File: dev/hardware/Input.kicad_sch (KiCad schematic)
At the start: 23 parts, among them J601 Conn_02x08_Top_Bottom, SW1 TILT SW, U601 74HC165, U602 74HC165

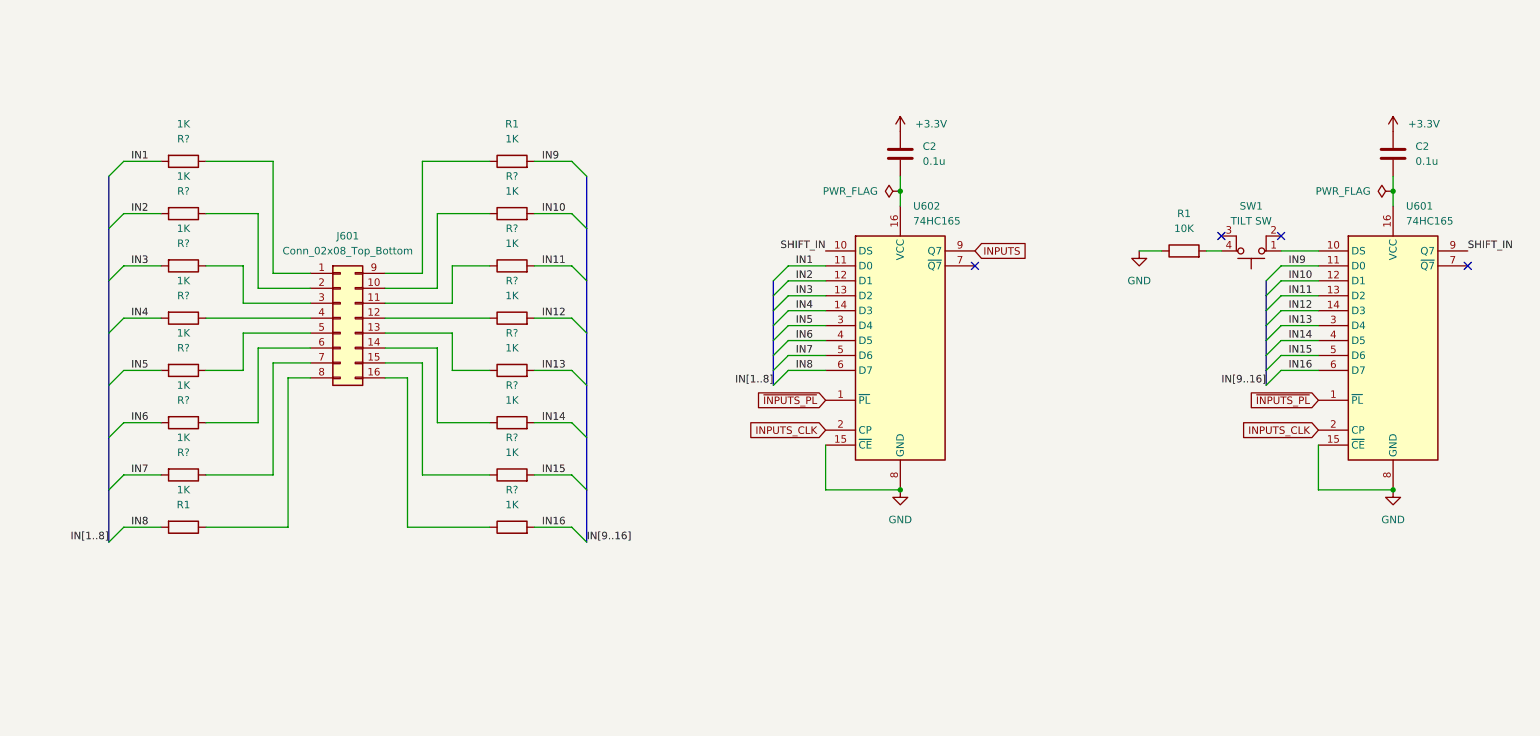
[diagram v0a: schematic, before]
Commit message: Started developing PCB layout
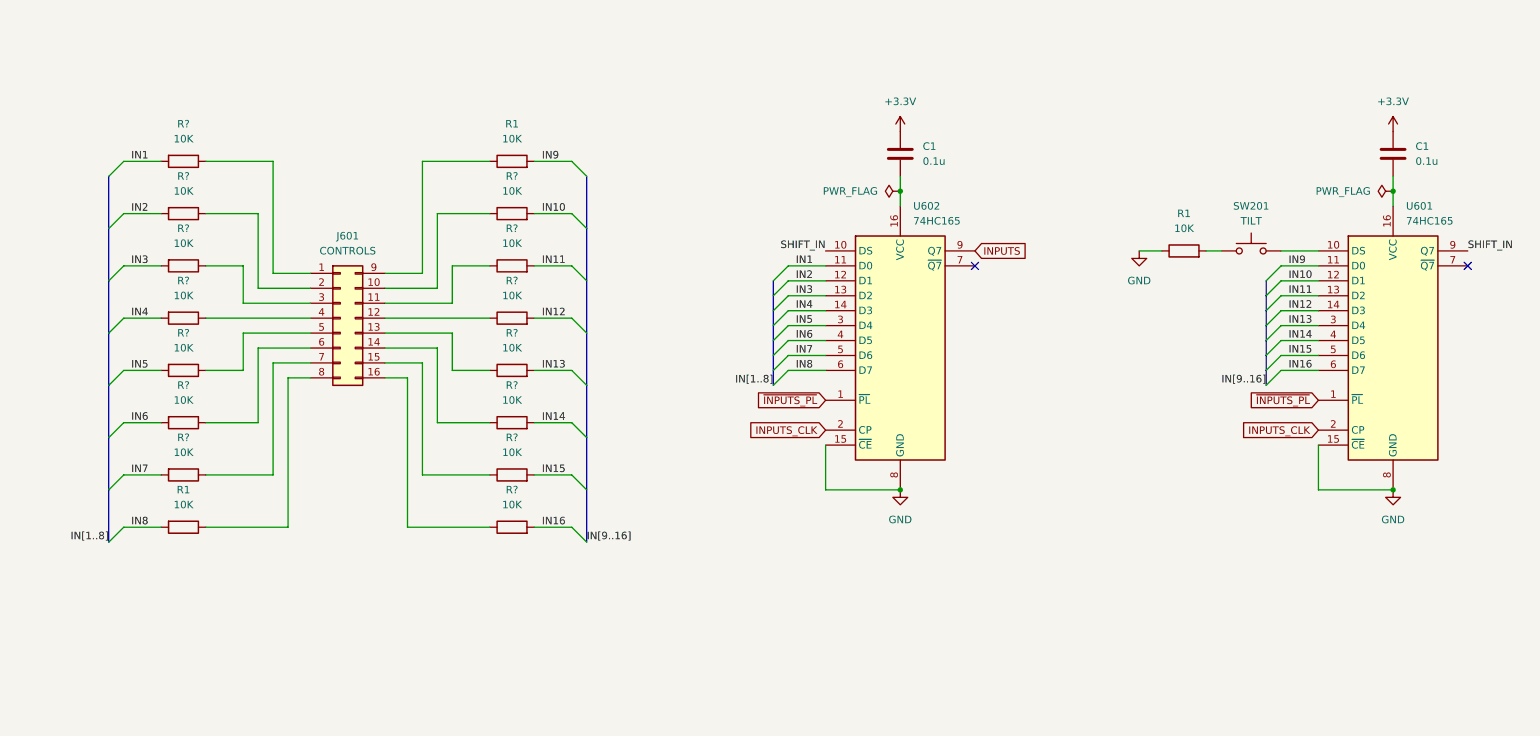
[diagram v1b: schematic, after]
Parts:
- removed C2 (x2): 0.1u, Capacitor_THT:C_Radial_D4.0mm_H7.0mm_P1.50mm, symbol Device:C
- removed SW1: TILT SW, Button_Switch_THT:SW_PUSH_6mm_H5mm, symbol Switch:SW_MEC_5E
- added C1 (x2): 0.1u, Capacitor_THT:C_Disc_D3.4mm_W2.1mm_P2.50mm, symbol Device:C
- added SW201: TILT, Button_Switch_THT:SW_PUSH_6mm_H5mm, symbol Switch:SW_Push
- J601: value Conn_02x08_Top_Bottom -> CONTROLS
- R1, R? (x14): value 1K -> 10K
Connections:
- net +3.3V: now also C1.2, C1.2
- net at U602.16 (VCC): now also C1.1
- net at U601.10 (DS): now also SW201.2
- net at R1.2: now also SW201.1
- net at U601.16 (VCC): now also C1.1
- no-connect marks 4 -> 2

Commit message: Fixed resistors and reset PCB
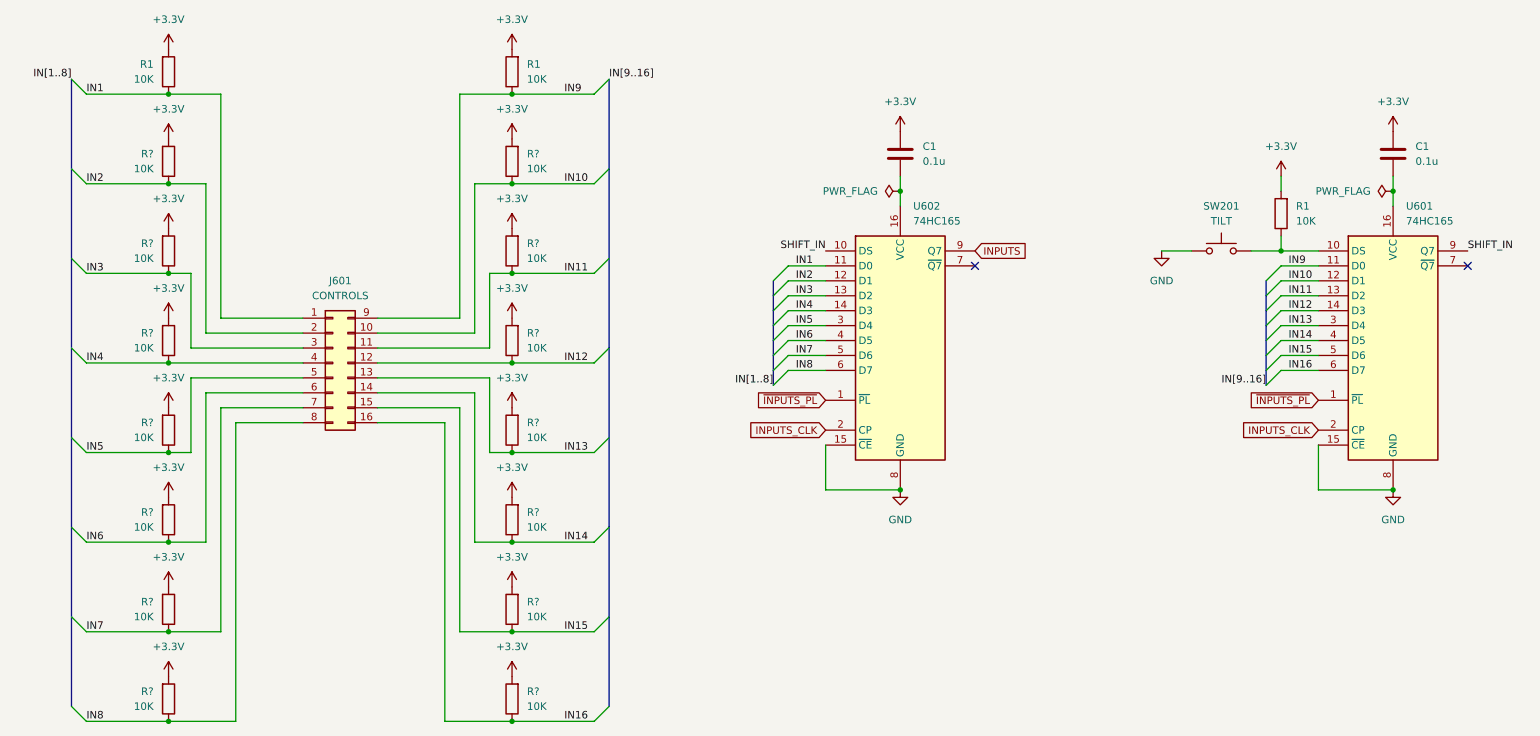
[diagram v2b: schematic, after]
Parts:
- removed R1 (x3), R? (x14): 10K, Resistor_THT:R_Axial_DIN0207_L6.3mm_D2.5mm_P10.16mm_Horizontal, symbol Device:R
- added R1 (x3), R? (x14): 10K, Resistor_THT:R_Axial_DIN0207_L6.3mm_D2.5mm_P10.16mm_Horizontal, symbol Device:R
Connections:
- net +3.3V: now also R1.2, R1.2, R1.2, R?.2, R?.2, R?.2, R?.2, R?.2, R?.2, R?.2, R?.2, R?.2, R?.2, R?.2, R?.2, R?.2, R?.2
- net GND: now also SW201.1
- net IN1: now also J601.1 (Pin_1), R1.1
- net IN10: now also J601.10 (Pin_10), R?.1
- net IN11: now also J601.11 (Pin_11), R?.1
- net IN12: now also J601.12 (Pin_12), R?.1
- net IN13: now also J601.13 (Pin_13), R?.1
- net IN14: now also J601.14 (Pin_14), R?.1
- net IN15: now also J601.15 (Pin_15), R?.1
- net IN16: now also J601.16 (Pin_16), R?.1
- net IN2: now also J601.2 (Pin_2), R?.1
- net IN3: now also J601.3 (Pin_3), R?.1
- net IN4: now also J601.4 (Pin_4), R?.1
- net IN5: now also J601.5 (Pin_5), R?.1
- net IN6: now also J601.6 (Pin_6), R?.1
- net IN7: now also J601.7 (Pin_7), R?.1
- net IN8: now also J601.8 (Pin_8), R?.1
- net IN9: now also J601.9 (Pin_9), R1.1
- net at SW201.2, U601.10 (DS): now also R1.1
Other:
- moved on the sheet: SW201

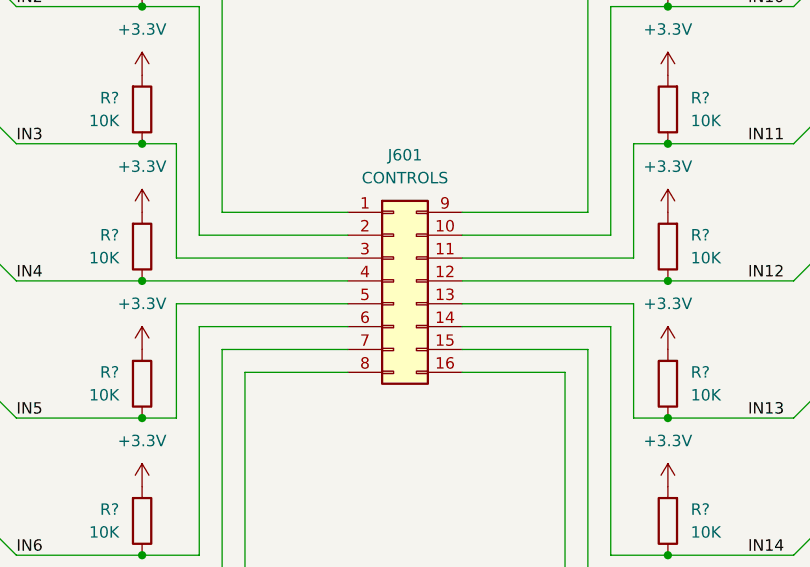
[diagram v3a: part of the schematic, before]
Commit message: Updated input header pinout
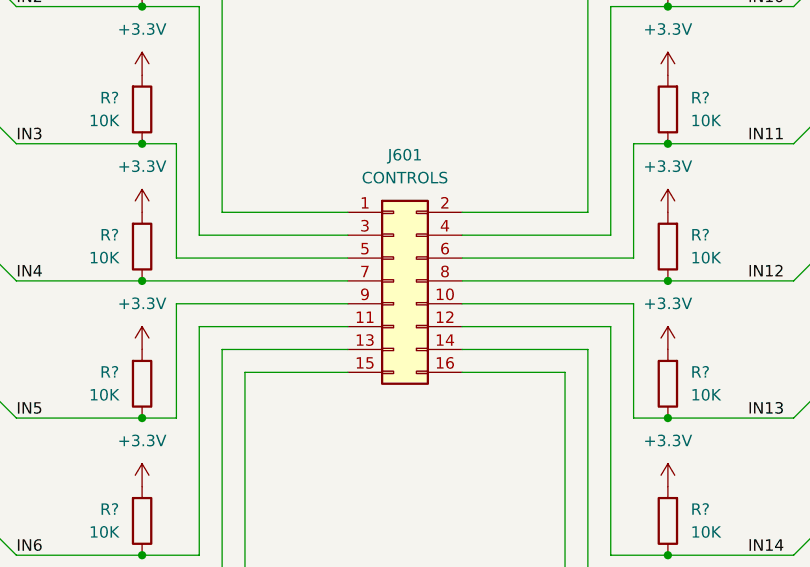
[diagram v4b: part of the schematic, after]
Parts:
- J601: symbol Connector_Generic:Conn_02x08_Top_Bottom -> Connector_Generic:Conn_02x08_Odd_Even
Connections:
- net IN10: now also J601.4 (Pin_4); no longer J601.10 (Pin_10)
- net IN11: now also J601.6 (Pin_6); no longer J601.11 (Pin_11)
- net IN12: now also J601.8 (Pin_8); no longer J601.12 (Pin_12)
- net IN13: now also J601.10 (Pin_10); no longer J601.13 (Pin_13)
- net IN14: now also J601.12 (Pin_12); no longer J601.14 (Pin_14)
- net IN15: now also J601.14 (Pin_14); no longer J601.15 (Pin_15)
- net IN2: now also J601.3 (Pin_3); no longer J601.2 (Pin_2)
- net IN3: now also J601.5 (Pin_5); no longer J601.3 (Pin_3)
- net IN4: now also J601.7 (Pin_7); no longer J601.4 (Pin_4)
- net IN5: now also J601.9 (Pin_9); no longer J601.5 (Pin_5)
- net IN6: now also J601.11 (Pin_11); no longer J601.6 (Pin_6)
- net IN7: now also J601.13 (Pin_13); no longer J601.7 (Pin_7)
- net IN8: now also J601.15 (Pin_15); no longer J601.8 (Pin_8)
- net IN9: now also J601.2 (Pin_2); no longer J601.9 (Pin_9)
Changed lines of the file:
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@@
     )
   )
-  (symbol (lib_id "Connector_Generic:Conn_02x08_Top_Bottom") (at 73.66 100.33 0) (unit 1)
+  (symbol (lib_id "Connector_Generic:Conn_02x08_Odd_Even") (at 73.66 100.33 0) (unit 1)
     (in_bom yes) (on_board yes) (dnp no) (fields_autoplaced)
     (property "Reference" "J601" (at 74.93 86.36 0)

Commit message: Finalized optimized board layout
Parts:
- removed R1 (x2), R? (x14): 10K, Resistor_THT:R_Axial_DIN0207_L6.3mm_D2.5mm_P10.16mm_Horizontal, symbol Device:R
- added RN601, RN602: 10K, Resistor_THT:R_Array_SIP9, symbol Device:R_Network08
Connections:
- net +3.3V: now also RN601.1 (common), RN602.1 (common)
- net IN1: now also RN601.2 (R1)
- net IN10: now also RN602.3 (R2)
- net IN11: now also RN602.4 (R3)
- net IN12: now also RN602.5 (R4)
- net IN13: now also RN602.6 (R5)
- net IN14: now also RN602.7 (R6)
- net IN15: now also RN602.8 (R7)
- net IN16: now also RN602.9 (R8)
- net IN2: now also RN601.3 (R2)
- net IN3: now also RN601.4 (R3)
- net IN4: now also RN601.5 (R4)
- net IN5: now also RN601.6 (R5)
- net IN6: now also RN601.7 (R6)
- net IN7: now also RN601.8 (R7)
- net IN8: now also RN601.9 (R8)
- net IN9: now also RN602.2 (R1)

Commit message: Finalized review schematic & pcb
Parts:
- removed C1 (x2): 0.1u, Capacitor_THT:C_Disc_D3.4mm_W2.1mm_P2.50mm, symbol Device:C
- added C1 (x2): 0.1u, Capacitor_THT:C_Disc_D3.4mm_W2.1mm_P2.50mm, symbol Device:C
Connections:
- net +3.3V: now also U601.16 (VCC), U602.16 (VCC), C1.2, C1.2
- net GND: now also C1.1, C1.1

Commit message: Thicc-traced VGA sig test - REVERT HERE
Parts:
- renumbered C1 to C?, R1 to R?, SW201 to SW?, U602 to U601, U601 to U602

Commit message: Finalized dev board administrivia
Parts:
- removed C? (x2): 0.1u, Capacitor_THT:C_Disc_D3.4mm_W2.1mm_P2.50mm, symbol Device:C
- removed R?: 10K, Resistor_THT:R_Axial_DIN0207_L6.3mm_D2.5mm_P10.16mm_Horizontal, symbol Device:R
- removed SW?: TILT, Button_Switch_THT:SW_PUSH_6mm_H5mm, symbol Switch:SW_Push
- added C? (x2): 0.1u, Capacitor_THT:C_Disc_D3.4mm_W2.1mm_P2.50mm, symbol Device:C
- added R?: 10K, Resistor_THT:R_Axial_DIN0207_L6.3mm_D2.5mm_P10.16mm_Horizontal, symbol Device:R
- added SW201: TILT, Button_Switch_THT:SW_PUSH_6mm_H5mm, symbol Switch:SW_Push
- J601: Part (none) -> PH2-16-UA
- RN601, RN602: Part (none) -> 4609M-101-103LF
- U601, U602: Part (none) -> SN74HC165N
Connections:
- net +3.3V: now also C?.2, C?.2, R?.2
- net GND: now also C?.1, C?.1, SW201.1
- net at U602.10 (DS): now also R?.1, SW201.2
